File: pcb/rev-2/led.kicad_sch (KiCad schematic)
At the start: 3 parts, among them U10 LP5810ADSDR

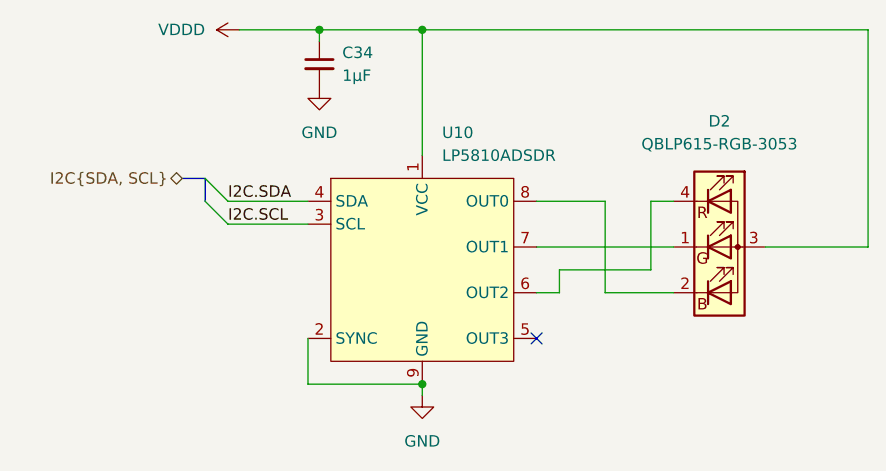
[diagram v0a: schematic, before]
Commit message: pcb: update
Mostly downsize several decoupling capacitors to save space
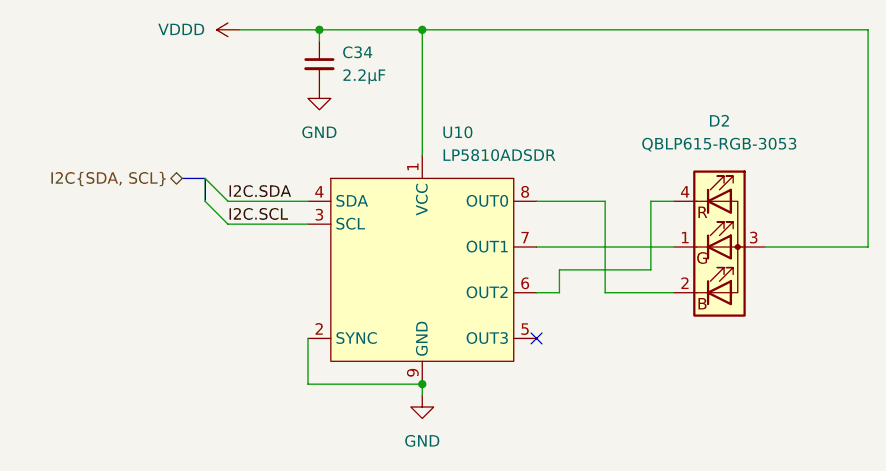
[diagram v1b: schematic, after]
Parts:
- C34: value 1µF -> 2.2µF; footprint Capacitor_SMD:C_0603_1608Metric -> zeus-le:C_0402_1005Metric_Silkscreen_Clearance; manf# CL10B105KP8NNNC -> GRM155R61A225ME01D
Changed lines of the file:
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@@
 			)
 		)
-		(property "Value" "1µF"
+		(property "Value" "2.2µF"
 			(at 119.38 78.7462 0)
 			(effects
@@
 			)
 		)
-		(property "Footprint" "Capacitor_SMD:C_0603_1608Metric"
+		(property "Footprint" "zeus-le:C_0402_1005Metric_Silkscreen_Clearance"
 			(at 116.84 77.47 0)
 			(effects
@@
 			)
 		)
-		(property "Description" "Capacitor, decoupling, 10V, X7R"
+		(property "Description" "Capacitor, decoupling, 10V, X5R"
 			(at 116.84 77.47 0)
 			(effects
@@
 			)
 		)
-		(property "manf#" "CL10B105KP8NNNC"
+		(property "manf#" "GRM155R61A225ME01D"
 			(at 116.84 77.47 0)
 			(effects
